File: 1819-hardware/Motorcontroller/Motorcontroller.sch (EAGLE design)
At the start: 33 parts, among them U1 GENERIC-SOIC8MSGEQ7N-FILTER, U2 GENERIC-SOIC8MSGEQ7N-FILTER, U3 GENERIC-SOIC8MSGEQ7N-FILTER

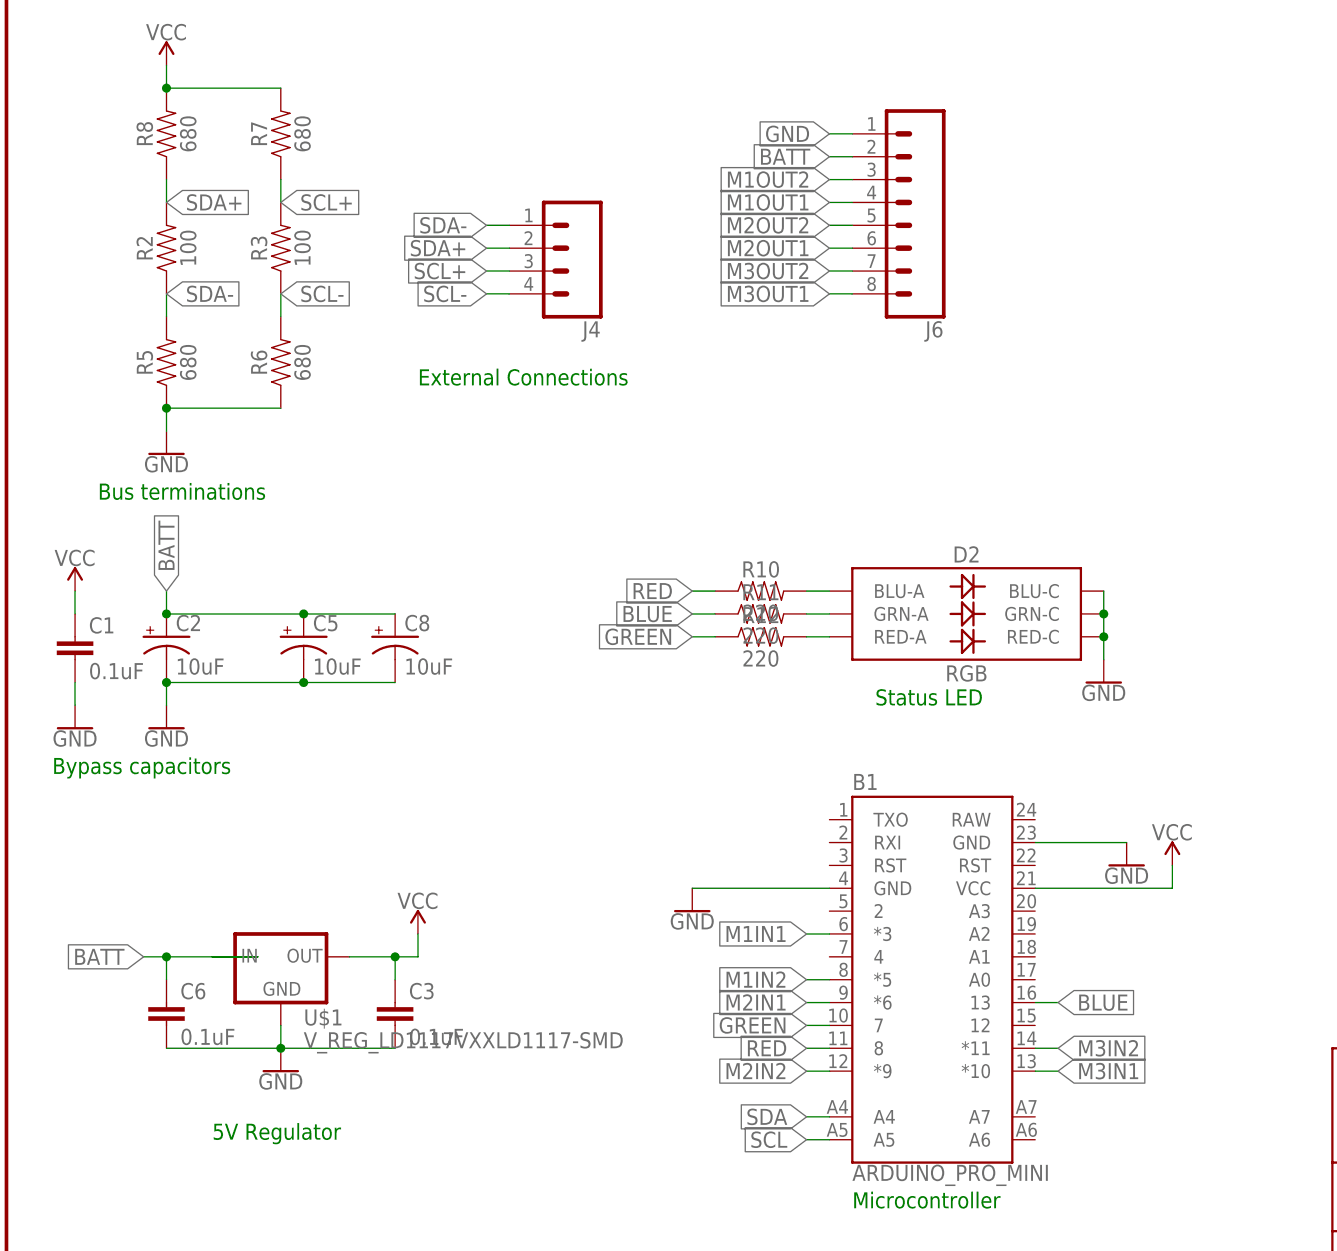
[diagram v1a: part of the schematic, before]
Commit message: more board routing
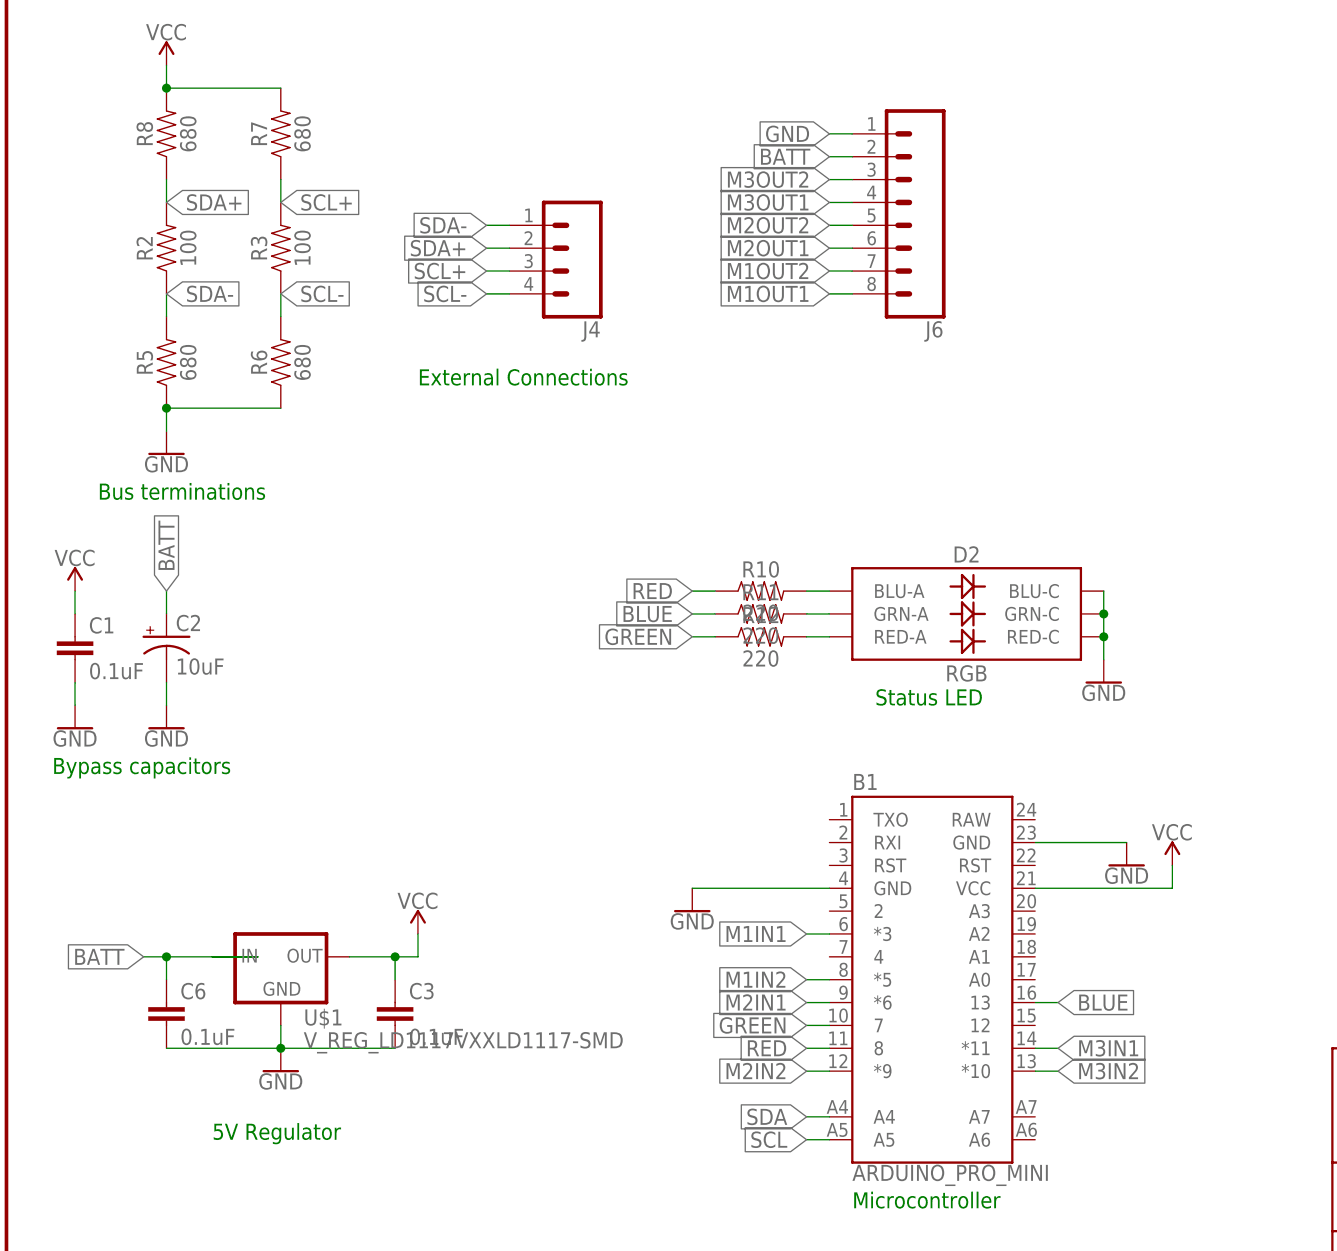
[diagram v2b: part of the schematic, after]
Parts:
- removed C5, C8: 10uF, SparkFun-Capacitors:10UF-POLAR-RADIAL-2.5MM-25V-20%
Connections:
- net BATT: no longer C5.+, C8.+
- net GND: no longer C5.-, C8.-
- net M1OUT1: now also J6.8; no longer J6.4
- net M1OUT2: now also J6.7; no longer J6.3
- net M3IN1: now also B1.*11; no longer B1.*10
- net M3IN2: now also B1.*10; no longer B1.*11
- net M3OUT1: now also J6.4; no longer J6.8
- net M3OUT2: now also J6.3; no longer J6.7
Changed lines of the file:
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@@
 <part name="U1" library="SparkFun-Retired" deviceset="GENERIC-SOIC8" device="MSGEQ7N-FILTER"/>
 <part name="C2" library="SparkFun-Capacitors" library_urn="urn:adsk.eagle:library:510" deviceset="10UF-POLAR" device="-RADIAL-2.5MM-25V-20%" package3d_urn="urn:adsk.eagle:package:37423/1" value="10uF"/>
-<part name="C5" library="SparkFun-Capacitors" library_urn="urn:adsk.eagle:library:510" deviceset="10UF-POLAR" device="-RADIAL-2.5MM-25V-20%" package3d_urn="urn:adsk.eagle:package:37423/1" value="10uF"/>
-<part name="C8" library="SparkFun-Capacitors" library_urn="urn:adsk.eagle:library:510" deviceset="10UF-POLAR" device="-RADIAL-2.5MM-25V-20%" package3d_urn="urn:adsk.eagle:package:37423/1" value="10uF"/>
 <part name="GND1" library="SparkFun-PowerSymbols" library_urn="urn:adsk.eagle:library:530" deviceset="GND" device=""/>
 <part name="GND2" library="SparkFun-PowerSymbols" library_urn="urn:adsk.eagle:library:530" deviceset="GND" device=""/>
@@
 <instance part="U1" gate="G$1" x="180.34" y="167.64"/>
 <instance part="C2" gate="G$1" x="17.78" y="81.28"/>
-<instance part="C5" gate="G$1" x="33.02" y="81.28"/>
-<instance part="C8" gate="G$1" x="43.18" y="81.28"/>
 <instance part="GND1" gate="1" x="172.72" y="167.64" rot="R270"/>
 <instance part="GND2" gate="1" x="200.66" y="165.1" rot="R90"/>
@@
 <segment>
 <pinref part="C2" gate="G$1" pin="-"/>
-<wire x1="17.78" y1="76.2" x2="33.02" y2="76.2" width="0.1524" layer="91"/>
-<pinref part="C5" gate="G$1" pin="-"/>
-<junction x="33.02" y="76.2"/>
-<pinref part="C8" gate="G$1" pin="-"/>
-<wire x1="33.02" y1="76.2" x2="43.18" y2="76.2" width="0.1524" layer="91"/>
 <wire x1="17.78" y1="76.2" x2="17.78" y2="73.66" width="0.1524" layer="91"/>
-<junction x="17.78" y="76.2"/>
 <pinref part="GND20" gate="1" pin="GND"/>
 </segment>
@@
 <segment>
 <pinref part="C2" gate="G$1" pin="+"/>
-<wire x1="17.78" y1="83.82" x2="33.02" y2="83.82" width="0.1524" layer="91"/>
-<pinref part="C5" gate="G$1" pin="+"/>
-<junction x="33.02" y="83.82"/>
-<pinref part="C8" gate="G$1" pin="+"/>
-<wire x1="33.02" y1="83.82" x2="43.18" y2="83.82" width="0.1524" layer="91"/>
 <wire x1="17.78" y1="83.82" x2="17.78" y2="86.36" width="0.1524" layer="91"/>
-<junction x="17.78" y="83.82"/>
 <label x="17.78" y="86.36" size="1.778" layer="95" rot="R90" xref="yes"/>
 </segment>
@@
 <net name="M3IN1" class="0">
 <segment>
+<pinref part="U3" gate="G$1" pin="3"/>
+<wire x1="177.8" y1="73.66" x2="175.26" y2="73.66" width="0.1524" layer="91"/>
+<label x="175.26" y="73.66" size="1.778" layer="95" rot="R180" xref="yes"/>
+</segment>
+<segment>
+<pinref part="B1" gate="G$1" pin="*11"/>
+<wire x1="114.3" y1="35.56" x2="116.84" y2="35.56" width="0.1524" layer="91"/>
+<label x="116.84" y="35.56" size="1.778" layer="95" xref="yes"/>
+</segment>
+</net>
+<net name="M3IN2" class="0">
+<segment>
+<pinref part="U3" gate="G$1" pin="2"/>
+<wire x1="177.8" y1="76.2" x2="175.26" y2="76.2" width="0.1524" layer="91"/>
+<label x="175.26" y="76.2" size="1.778" layer="95" rot="R180" xref="yes"/>
+</segment>
+<segment>
 <pinref part="B1" gate="G$1" pin="*10"/>
 <wire x1="114.3" y1="33.02" x2="116.84" y2="33.02" width="0.1524" layer="91"/>
 <label x="116.84" y="33.02" size="1.778" layer="95" xref="yes"/>
 </segment>
-<segment>
-<pinref part="U3" gate="G$1" pin="3"/>
-<wire x1="177.8" y1="73.66" x2="175.26" y2="73.66" width="0.1524" layer="91"/>
-<label x="175.26" y="73.66" size="1.778" layer="95" rot="R180" xref="yes"/>
-</segment>
-</net>
-<net name="M3IN2" class="0">
-<segment>
-<pinref part="B1" gate="G$1" pin="*11"/>
-<wire x1="114.3" y1="35.56" x2="116.84" y2="35.56" width="0.1524" layer="91"/>
-<label x="116.84" y="35.56" size="1.778" layer="95" xref="yes"/>
-</segment>
-<segment>
-<pinref part="U3" gate="G$1" pin="2"/>
-<wire x1="177.8" y1="76.2" x2="175.26" y2="76.2" width="0.1524" layer="91"/>
-<label x="175.26" y="76.2" size="1.778" layer="95" rot="R180" xref="yes"/>
-</segment>
 </net>
 <net name="N$7" class="0">
@@
 </segment>
 <segment>
+<pinref part="J6" gate="G$1" pin="7"/>
+<wire x1="93.98" y1="121.92" x2="91.44" y2="121.92" width="0.1524" layer="91"/>
+<label x="91.44" y="121.92" size="1.778" layer="95" rot="R180" xref="yes"/>
+</segment>
+</net>
+<net name="M1OUT1" class="0">
+<segment>
+<pinref part="U1" gate="G$1" pin="6"/>
+<wire x1="195.58" y1="162.56" x2="198.12" y2="162.56" width="0.1524" layer="91"/>
+<label x="198.12" y="162.56" size="1.778" layer="95" xref="yes"/>
+</segment>
+<segment>
+<pinref part="J6" gate="G$1" pin="8"/>
+<wire x1="93.98" y1="119.38" x2="91.44" y2="119.38" width="0.1524" layer="91"/>
+<label x="91.44" y="119.38" size="1.778" layer="95" rot="R180" xref="yes"/>
+</segment>
+</net>
+<net name="N$1" class="0">
+<segment>
+<pinref part="U2" gate="G$1" pin="4"/>
+<wire x1="177.8" y1="116.84" x2="175.26" y2="116.84" width="0.1524" layer="91"/>
+<pinref part="R13" gate="G$1" pin="2"/>
+</segment>
+</net>
+<net name="N$2" class="0">
+<segment>
+<pinref part="U3" gate="G$1" pin="4"/>
+<wire x1="177.8" y1="71.12" x2="175.26" y2="71.12" width="0.1524" layer="91"/>
+<pinref part="R14" gate="G$1" pin="2"/>
+</segment>
+</net>
+<net name="M2OUT2" class="0">
+<segment>
+<pinref part="U2" gate="G$1" pin="8"/>
+<wire x1="195.58" y1="124.46" x2="198.12" y2="124.46" width="0.1524" layer="91"/>
+<label x="198.12" y="124.46" size="1.778" layer="95" xref="yes"/>
+</segment>
+<segment>
+<pinref part="J6" gate="G$1" pin="5"/>
+<wire x1="93.98" y1="127" x2="91.44" y2="127" width="0.1524" layer="91"/>
+<label x="91.44" y="127" size="1.778" layer="95" rot="R180" xref="yes"/>
+</segment>
+</net>
+<net name="M2OUT1" class="0">
+<segment>
+<pinref part="U2" gate="G$1" pin="6"/>
+<wire x1="195.58" y1="119.38" x2="198.12" y2="119.38" width="0.1524" layer="91"/>
+<label x="198.12" y="119.38" size="1.778" layer="95" xref="yes"/>
+</segment>
+<segment>
+<pinref part="J6" gate="G$1" pin="6"/>
+<wire x1="93.98" y1="124.46" x2="91.44" y2="124.46" width="0.1524" layer="91"/>
+<label x="91.44" y="124.46" size="1.778" layer="95" rot="R180" xref="yes"/>
+</segment>
+</net>
+<net name="M3OUT2" class="0">
+<segment>
+<pinref part="U3" gate="G$1" pin="8"/>
+<wire x1="195.58" y1="78.74" x2="198.12" y2="78.74" width="0.1524" layer="91"/>
+<label x="198.12" y="78.74" size="1.778" layer="95" xref="yes"/>
+</segment>
+<segment>
 <pinref part="J6" gate="G$1" pin="3"/>
 <wire x1="93.98" y1="132.08" x2="91.44" y2="132.08" width="0.1524" layer="91"/>
@@
 </segment>
 </net>
-<net name="M1OUT1" class="0">
-<segment>
-<pinref part="U1" gate="G$1" pin="6"/>
-<wire x1="195.58" y1="162.56" x2="198.12" y2="162.56" width="0.1524" layer="91"/>
-<label x="198.12" y="162.56" size="1.778" layer="95" xref="yes"/>
+<net name="M3OUT1" class="0">
+<segment>
+<pinref part="U3" gate="G$1" pin="6"/>
+<wire x1="195.58" y1="73.66" x2="198.12" y2="73.66" width="0.1524" layer="91"/>
+<label x="198.12" y="73.66" size="1.778" layer="95" xref="yes"/>
 </segment>
 <segment>
@@
 </segment>
 </net>
-<net name="N$1" class="0">
-<segment>
-<pinref part="U2" gate="G$1" pin="4"/>
-<wire x1="177.8" y1="116.84" x2="175.26" y2="116.84" width="0.1524" layer="91"/>
-<pinref part="R13" gate="G$1" pin="2"/>
-</segment>
-</net>
-<net name="N$2" class="0">
-<segment>
-<pinref part="U3" gate="G$1" pin="4"/>
-<wire x1="177.8" y1="71.12" x2="175.26" y2="71.12" width="0.1524" layer="91"/>
-<pinref part="R14" gate="G$1" pin="2"/>
-</segment>
-</net>
-<net name="M2OUT2" class="0">
-<segment>
-<pinref part="U2" gate="G$1" pin="8"/>
-<wire x1="195.58" y1="124.46" x2="198.12" y2="124.46" width="0.1524" layer="91"/>
-<label x="198.12" y="124.46" size="1.778" layer="95" xref="yes"/>
-</segment>
-<segment>
-<pinref part="J6" gate="G$1" pin="5"/>
-<wire x1="93.98" y1="127" x2="91.44" y2="127" width="0.1524" layer="91"/>
-<label x="91.44" y="127" size="1.778" layer="95" rot="R180" xref="yes"/>
-</segment>
-</net>
-<net name="M2OUT1" class="0">
-<segment>
-<pinref part="U2" gate="G$1" pin="6"/>
-<wire x1="195.58" y1="119.38" x2="198.12" y2="119.38" width="0.1524" layer="91"/>
-<label x="198.12" y="119.38" size="1.778" layer="95" xref="yes"/>
-</segment>
-<segment>
-<pinref part="J6" gate="G$1" pin="6"/>
-<wire x1="93.98" y1="124.46" x2="91.44" y2="124.46" width="0.1524" layer="91"/>
-<label x="91.44" y="124.46" size="1.778" layer="95" rot="R180" xref="yes"/>
-</segment>
-</net>
-<net name="M3OUT2" class="0">
-<segment>
-<pinref part="U3" gate="G$1" pin="8"/>
-<wire x1="195.58" y1="78.74" x2="198.12" y2="78.74" width="0.1524" layer="91"/>
-<label x="198.12" y="78.74" size="1.778" layer="95" xref="yes"/>
-</segment>
-<segment>
-<pinref part="J6" gate="G$1" pin="7"/>
-<wire x1="93.98" y1="121.92" x2="91.44" y2="121.92" width="0.1524" layer="91"/>
-<label x="91.44" y="121.92" size="1.778" layer="95" rot="R180" xref="yes"/>
-</segment>
-</net>
-<net name="M3OUT1" class="0">
-<segment>
-<pinref part="U3" gate="G$1" pin="6"/>
-<wire x1="195.58" y1="73.66" x2="198.12" y2="73.66" width="0.1524" layer="91"/>
-<label x="198.12" y="73.66" size="1.778" layer="95" xref="yes"/>
-</segment>
-<segment>
-<pinref part="J6" gate="G$1" pin="8"/>
-<wire x1="93.98" y1="119.38" x2="91.44" y2="119.38" width="0.1524" layer="91"/>
-<label x="91.44" y="119.38" size="1.778" layer="95" rot="R180" xref="yes"/>
-</segment>
-</net>

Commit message: worked on routing
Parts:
- added J1, J7, J8: (no value), SparkFun-Connectors:CONN_01PTH_NO_SILK_YES_STOP
- FRAME1: value FRAME-LETTER -> FRAME-LETTERNO_PACKAGE; device SparkFun-Aesthetics:FRAME-LETTER -> SparkFun-Aesthetics:FRAME-LETTERNO_PACKAGE
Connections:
- net BATT: now also J1.1, J7.1, J8.1
- net GREEN: now also B1.A0; no longer B1.7
- net RED: now also B1.A1; no longer B1.8
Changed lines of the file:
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@@
 <parts>
 <part name="B1" library="SparkFun-Boards" deviceset="ARDUINO_PRO_MINI" device=""/>
-<part name="FRAME1" library="SparkFun-Aesthetics" deviceset="FRAME-LETTER" device=""/>
+<part name="FRAME1" library="SparkFun-Aesthetics" deviceset="FRAME-LETTER" device="NO_PACKAGE" value="FRAME-LETTERNO_PACKAGE"/>
 <part name="J4" library="SparkFun-Connectors" library_urn="urn:adsk.eagle:library:513" deviceset="CONN_04" device="" package3d_urn="urn:adsk.eagle:package:38085/1"/>
 <part name="C1" library="SparkFun-Capacitors" library_urn="urn:adsk.eagle:library:510" deviceset="0.1UF" device="-0603-25V-(+80/-20%)" package3d_urn="urn:adsk.eagle:package:37414/1" value="0.1uF"/>
@@
 <part name="C3" library="SparkFun-Capacitors" library_urn="urn:adsk.eagle:library:510" deviceset="0.1UF" device="-0603-25V-(+80/-20%)" package3d_urn="urn:adsk.eagle:package:37414/1" value="0.1uF"/>
 <part name="GND20" library="SparkFun-PowerSymbols" deviceset="GND" device=""/>
+<part name="J1" library="SparkFun-Connectors" library_urn="urn:adsk.eagle:library:513" deviceset="CONN_01" device="PTH_NO_SILK_YES_STOP" package3d_urn="urn:adsk.eagle:package:38041/1"/>
+<part name="J7" library="SparkFun-Connectors" library_urn="urn:adsk.eagle:library:513" deviceset="CONN_01" device="PTH_NO_SILK_YES_STOP" package3d_urn="urn:adsk.eagle:package:38041/1"/>
+<part name="J8" library="SparkFun-Connectors" library_urn="urn:adsk.eagle:library:513" deviceset="CONN_01" device="PTH_NO_SILK_YES_STOP" package3d_urn="urn:adsk.eagle:package:38041/1"/>
 </parts>
 <sheets>
@@
 <instance part="C3" gate="G$1" x="43.18" y="38.1"/>
 <instance part="GND20" gate="1" x="17.78" y="71.12"/>
+<instance part="J1" gate="G$1" x="205.74" y="177.8"/>
+<instance part="J7" gate="G$1" x="205.74" y="134.62"/>
+<instance part="J8" gate="G$1" x="205.74" y="88.9"/>
 </instances>
 <busses>
@@
 </segment>
 <segment>
-<pinref part="B1" gate="G$1" pin="8"/>
-<wire x1="91.44" y1="35.56" x2="88.9" y2="35.56" width="0.1524" layer="91"/>
-<label x="88.9" y="35.56" size="1.778" layer="95" rot="R180" xref="yes"/>
+<pinref part="B1" gate="G$1" pin="A1"/>
+<wire x1="114.3" y1="45.72" x2="116.84" y2="45.72" width="0.1524" layer="91"/>
+<label x="116.84" y="45.72" size="1.778" layer="95" xref="yes"/>
 </segment>
 </net>
@@
 </segment>
 <segment>
-<pinref part="B1" gate="G$1" pin="7"/>
-<wire x1="91.44" y1="38.1" x2="88.9" y2="38.1" width="0.1524" layer="91"/>
-<label x="88.9" y="38.1" size="1.778" layer="95" rot="R180" xref="yes"/>
+<pinref part="B1" gate="G$1" pin="A0"/>
+<wire x1="114.3" y1="43.18" x2="116.84" y2="43.18" width="0.1524" layer="91"/>
+<label x="116.84" y="43.18" size="1.778" layer="95" xref="yes"/>
 </segment>
 </net>
@@
 <label x="15.24" y="45.72" size="1.778" layer="95" rot="R180" xref="yes"/>
 </segment>
-</net>
+<segment>
+<pinref part="J1" gate="G$1" pin="1"/>
+<wire x1="213.36" y1="177.8" x2="215.9" y2="177.8" width="0.1524" layer="91"/>
+<label x="215.9" y="177.8" size="1.778" layer="95" xref="yes"/>
+</segment>
+<segment>
+<pinref part="J7" gate="G$1" pin="1"/>
+<wire x1="213.36" y1="134.62" x2="215.9" y2="134.62" width="0.1524" layer="91"/>
+<label x="215.9" y="134.62" size="1.778" layer="95" xref="yes"/>
+</segment>
+<segment>
+<pinref part="J8" gate="G$1" pin="1"/>
+<wire x1="213.36" y1="88.9" x2="215.9" y2="88.9" width="0.1524" layer="91"/>
+<label x="215.9" y="88.9" size="1.778" layer="95" xref="yes"/>
+</segment>
+</net>
